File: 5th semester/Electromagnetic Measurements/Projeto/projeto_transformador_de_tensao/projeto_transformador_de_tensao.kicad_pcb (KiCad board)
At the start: 2 copper layers, 12 parts

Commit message: Update tension transformer
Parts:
- removed the REF** at (76.2, 17.8)
- removed the REF** at (33.0, 15.2)
- removed the REF** at (61.0, 27.9)
- removed the REF** at (81.3, 15.2)
- removed the REF** at (20.3, 35.6)
- removed the REF** at (71.2, 25.4)
- removed the REF** at (33.0, 22.9)
- removed the REF** at (32.9, 40.6)
- removed the REF** at (32.9, 33.0)
- added 220uF: CP_Radial_D10.0mm_P5.00mm, Capacitor_THT:CP_Radial_D10.0mm_P5.00mm, F.Cu at (44.5, 43.7)
- added 220uF: CP_Radial_D10.0mm_P5.00mm, Capacitor_THT:CP_Radial_D10.0mm_P5.00mm, F.Cu at (44.5, 38.7)
- added REF**: R_Axial_DIN0204_L3.6mm_D1.6mm_P7.62mm_Horizontal, Resistor_THT:R_Axial_DIN0204_L3.6mm_D1.6mm_P7.62mm_Horizontal, F.Cu at (47.0, 19.1)
- added REF**: D_A-405_P7.62mm_Horizontal, Diode_THT:D_A-405_P7.62mm_Horizontal, F.Cu at (25.4, 34.3)
- added REF**: D_A-405_P7.62mm_Horizontal, Diode_THT:D_A-405_P7.62mm_Horizontal, F.Cu at (25.4, 44.4)
- added REF**: Pin_D0.9mm_L10.0mm_W2.4mm_FlatFork, Connector_Pin:Pin_D0.9mm_L10.0mm_W2.4mm_FlatFork, F.Cu at (47.0, 15.2)
- added REF**: Pin_D0.9mm_L10.0mm_W2.4mm_FlatFork, Connector_Pin:Pin_D0.9mm_L10.0mm_W2.4mm_FlatFork, F.Cu at (21.6, 39.4)
- added REF**: D_A-405_P7.62mm_Horizontal, Diode_THT:D_A-405_P7.62mm_Horizontal, F.Cu at (25.5, 25.4)
- added REF**: D_A-405_P7.62mm_Horizontal, Diode_THT:D_A-405_P7.62mm_Horizontal, F.Cu at (25.5, 15.2)
- added REF**: R_Axial_DIN0204_L3.6mm_D1.6mm_P7.62mm_Horizontal, Resistor_THT:R_Axial_DIN0204_L3.6mm_D1.6mm_P7.62mm_Horizontal, F.Cu at (44.5, 22.9)
- added REF**: R_Axial_DIN0204_L3.6mm_D1.6mm_P7.62mm_Horizontal, Resistor_THT:R_Axial_DIN0204_L3.6mm_D1.6mm_P7.62mm_Horizontal, F.Cu at (29.2, 34.3)
- moved REF** 28.0 mm to (30.5, 19.1)
- moved 220uF 14.0 mm to (34.3, 26.8)
- moved REF** 1.34 mm to (21.7, 20.3)
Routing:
- net (no net): track 239.4 -> 188.0 mm

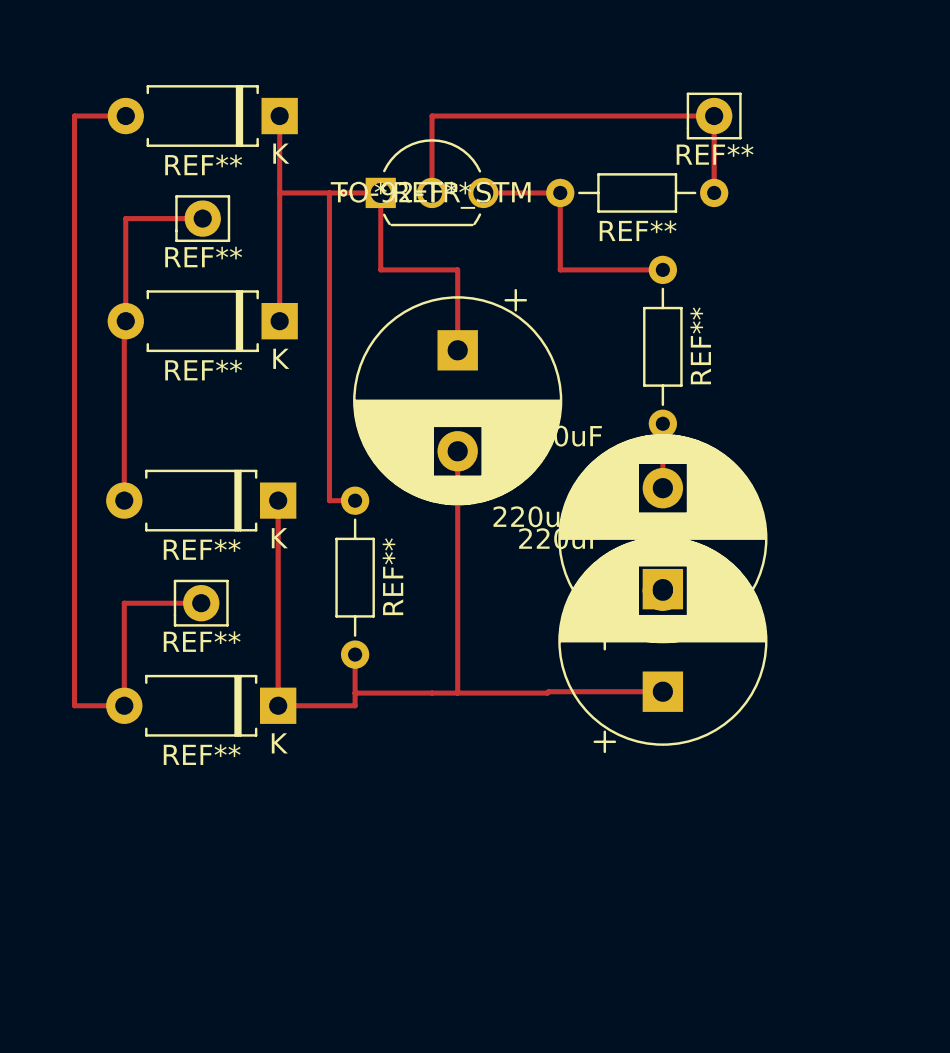
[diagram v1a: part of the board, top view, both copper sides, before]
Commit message: Final design for electromag measurements ac to dc transformer
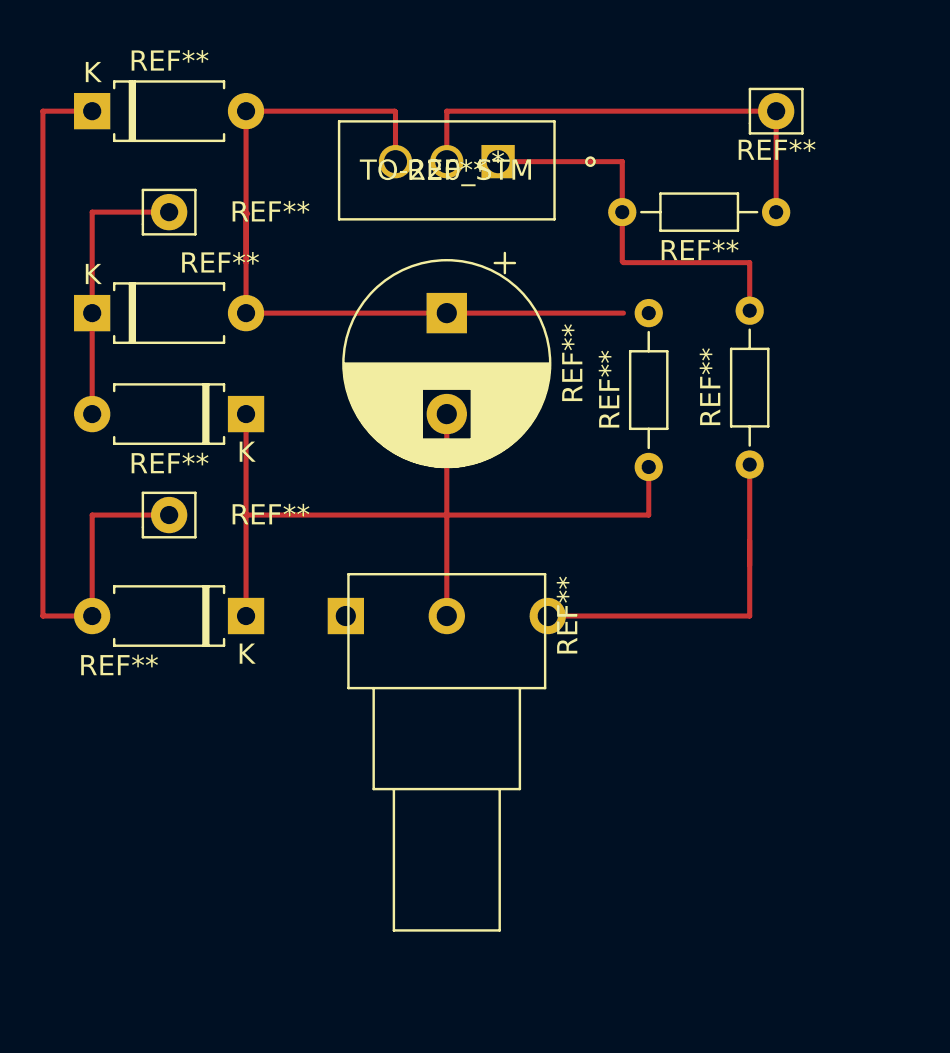
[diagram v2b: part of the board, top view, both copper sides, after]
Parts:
- removed 220uF (x3): CP_Radial_D10.0mm_P5.00mm, Capacitor_THT:CP_Radial_D10.0mm_P5.00mm
- removed the REF** at (30.5, 19.1)
- removed the REF** at (47.0, 19.1)
- removed the REF** at (25.4, 34.3)
- removed the REF** at (25.4, 44.4)
- removed the REF** at (47.0, 15.2)
- removed the REF** at (21.6, 39.4)
- removed the REF** at (25.5, 25.4)
- removed the REF** at (21.7, 20.3)
- removed the REF** at (25.5, 15.2)
- removed the REF** at (44.5, 22.9)
- removed the REF** at (29.2, 34.3)
- added REF**: D_A-405_P7.62mm_Horizontal, Diode_THT:D_A-405_P7.62mm_Horizontal, F.Cu at (23.8, 40.0)
- added REF**: R_Axial_DIN0204_L3.6mm_D1.6mm_P7.62mm_Horizontal, Resistor_THT:R_Axial_DIN0204_L3.6mm_D1.6mm_P7.62mm_Horizontal, F.Cu at (48.8, 32.5)
- added REF**: D_A-405_P7.62mm_Horizontal, Diode_THT:D_A-405_P7.62mm_Horizontal, F.Cu at (16.2, 15.0)
- added REF**: Pin_D0.9mm_L10.0mm_W2.4mm_FlatFork, Connector_Pin:Pin_D0.9mm_L10.0mm_W2.4mm_FlatFork, F.Cu at (50.1, 15.0)
- added REF**: D_A-405_P7.62mm_Horizontal, Diode_THT:D_A-405_P7.62mm_Horizontal, F.Cu at (16.2, 25.0)
- added REF**: Pin_D0.9mm_L10.0mm_W2.4mm_FlatFork, Connector_Pin:Pin_D0.9mm_L10.0mm_W2.4mm_FlatFork, F.Cu at (20.0, 20.0)
- added REF**: CP_Radial_D10.0mm_P5.00mm, Capacitor_THT:CP_Radial_D10.0mm_P5.00mm, F.Cu at (33.8, 25.0)
- added REF**: Potentiometer_Alps_RK09Y11_Single_Horizontal, Potentiometer_THT:Potentiometer_Alps_RK09Y11_Single_Horizontal, F.Cu at (31.2, 40.0)
- added REF**: R_Axial_DIN0204_L3.6mm_D1.6mm_P7.62mm_Horizontal, Resistor_THT:R_Axial_DIN0204_L3.6mm_D1.6mm_P7.62mm_Horizontal, F.Cu at (43.8, 32.6)
- added REF**: R_Axial_DIN0204_L3.6mm_D1.6mm_P7.62mm_Horizontal, Resistor_THT:R_Axial_DIN0204_L3.6mm_D1.6mm_P7.62mm_Horizontal, F.Cu at (50.1, 20.0)
- added REF**: D_A-405_P7.62mm_Horizontal, Diode_THT:D_A-405_P7.62mm_Horizontal, F.Cu at (23.8, 30.0)
- added REF**: Pin_D0.9mm_L10.0mm_W2.4mm_FlatFork, Connector_Pin:Pin_D0.9mm_L10.0mm_W2.4mm_FlatFork, F.Cu at (20.0, 35.0)
- added REF**: TO-220_STM, footprints:LM317T, F.Cu at (36.3, 17.5)
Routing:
- net (no net): track 188.0 -> 206.4 mm

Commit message: Backup point
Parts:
- added REF**: Pin_D0.9mm_L10.0mm_W2.4mm_FlatFork, Connector_Pin:Pin_D0.9mm_L10.0mm_W2.4mm_FlatFork, F.Cu at (46.2, 37.5)
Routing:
- net (no net): track 206.4 -> 211.4 mm
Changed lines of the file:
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@@
   )
   (net 0 "")
+  (footprint "Connector_Pin:Pin_D0.9mm_L10.0mm_W2.4mm_FlatFork" (layer "F.Cu")
+    (at 46.25 37.5)
+    (descr "solder Pin_ with flat fork, hole diameter 0.9mm, length 10.0mm, width 2.4mm")
+    (tags "solder Pin_ with flat fork")
+    (attr through_hole)
+    (fp_text reference "REF**" (at 0 1.95) (layer "F.SilkS")
+        (effects (font (size 1 1) (thickness 0.15)))
+    )
+    (fp_text value "Pin_D0.9mm_L10.0mm_W2.4mm_FlatFork" (at 0 -2.05) (layer "F.Fab") hide
+        (effects (font (size 1 1) (thickness 0.15)))
+    )
+    (fp_text user "${REFERENCE}" (at 0 1.95) (layer "F.Fab")
+        (effects (font (size 1 1) (thickness 0.15)))
+    )
+    (fp_line (start -1.3 -1.1) (end -1.3 0.6)
+      (stroke (width 0.12) (type solid)) (layer "F.SilkS"))
+    (fp_line (start -1.3 0.6) (end -1.3 1.1)
+      (stroke (width 0.12) (type solid)) (layer "F.SilkS"))
+    (fp_line (start -1.3 1.1) (end 1.3 1.1)
+      (stroke (width 0.12) (type solid)) (layer "F.SilkS"))
+    (fp_line (start 1.3 -1.1) (end -1.3 -1.1)
+      (stroke (width 0.12) (type solid)) (layer "F.SilkS"))
+    (fp_line (start 1.3 1.1) (end 1.3 -1.1)
+      (stroke (width 0.12) (type solid)) (layer "F.SilkS"))
+    (fp_line (start -1.7 -1.4) (end -1.7 1.4)
+      (stroke (width 0.05) (type solid)) (layer "F.CrtYd"))
+    (fp_line (start -1.7 -1.4) (end 1.7 -1.4)
+      (stroke (width 0.05) (type solid)) (layer "F.CrtYd"))
+    (fp_line (start 1.7 1.4) (end -1.7 1.4)
+      (stroke (width 0.05) (type solid)) (layer "F.CrtYd"))
+    (fp_line (start 1.7 1.4) (end 1.7 -1.4)
+      (stroke (width 0.05) (type solid)) (layer "F.CrtYd"))
+    (fp_line (start -1.2 -0.25) (end -1.2 0.25)
+      (stroke (width 0.12) (type solid)) (layer "F.Fab"))
+    (fp_line (start -1.2 0.25) (end 1.2 0.25)
+      (stroke (width 0.12) (type solid)) (layer "F.Fab"))
+    (fp_line (start 1.2 -0.25) (end -1.2 -0.25)
+      (stroke (width 0.12) (type solid)) (layer "F.Fab"))
+    (fp_line (start 1.2 0.25) (end 1.2 -0.25)
+      (stroke (width 0.12) (type solid)) (layer "F.Fab"))
+    (pad "1" thru_hole circle (at 0 0) (size 1.8 1.8) (drill 0.9) (layers "*.Cu" "*.Mask"))
+    (model "${KICAD6_3DMODEL_DIR}/Connector_Pin.3dshapes/Pin_D0.9mm_L10.0mm_W2.4mm_FlatFork.wrl"
+      (offset (xyz 0 0 0))
+      (scale (xyz 1 1 1))
+      (rotate (xyz 0 0 0))
+    )
+  )
   (footprint "Diode_THT:D_A-405_P7.62mm_Horizontal" (layer "F.Cu")
     (at 23.81 40 180)
@@
         (effects (font (size 1 1) (thickness 0.15)))
     )
+    (fp_text user "${REFERENCE}" (at 4.2 0) (layer "F.Fab")
+        (effects (font (size 1 1) (thickness 0.15)))
+    )
     (fp_text user "K" (at 0 -1.9) (layer "F.Fab")
-        (effects (font (size 1 1) (thickness 0.15)))
-    )
-    (fp_text user "${REFERENCE}" (at 4.2 0) (layer "F.Fab")
         (effects (font (size 1 1) (thickness 0.15)))
     )
@@
         (effects (font (size 1 1) (thickness 0.15)))
     )
+    (fp_text user "${REFERENCE}" (at 4.2 0) (layer "F.Fab")
+        (effects (font (size 1 1) (thickness 0.15)))
+    )
     (fp_text user "K" (at 0 -1.9) (layer "F.Fab")
-        (effects (font (size 1 1) (thickness 0.15)))
-    )
-    (fp_text user "${REFERENCE}" (at 4.2 0) (layer "F.Fab")
         (effects (font (size 1 1) (thickness 0.15)))
     )
@@
   (segment (start 42.5 22.5) (end 42.44 22.44) (width 0.25) (layer "F.Cu") (net 0))
   (segment (start 36.29 17.5) (end 42.44 17.5) (width 0.25) (layer "F.Cu") (net 0))
+  (segment (start 43.75 35) (end 43.75 37.5) (width 0.25) (layer "F.Cu") (net 0))
   (segment (start 23.81 40) (end 23.81 35) (width 0.25) (layer "F.Cu") (net 0))
   (segment (start 16.19 30) (end 16.19 25) (width 0.25) (layer "F.Cu") (net 0))
@@
   (segment (start 104.14 198.12) (end 106.68 198.12) (width 0.25) (layer "F.Cu") (net 0))
   (segment (start 31.17 15) (end 23.81 15) (width 0.25) (layer "F.Cu") (net 0))
+  (segment (start 43.75 37.5) (end 46.25 37.5) (width 0.25) (layer "F.Cu") (net 0))
   (segment (start 33.75 35) (end 33.75 30) (width 0.25) (layer "F.Cu") (net 0))
   (segment (start 16.19 35) (end 20 35) (width 0.25) (layer "F.Cu") (net 0))

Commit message: Update circuits lab report 5
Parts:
- moved Vout 0.06 mm to (50.0, 15.0)
- renumbered REF** to GND, REF** to Vin, REF** to Vout
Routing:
- net (no net): track 211.4 -> 213.7 mm
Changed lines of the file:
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@@
     (tags "solder Pin_ with flat fork")
     (attr through_hole)
-    (fp_text reference "REF**" (at 0 1.95) (layer "F.SilkS")
+    (fp_text reference "GND" (at 0 1.95) (layer "F.SilkS")
         (effects (font (size 1 1) (thickness 0.15)))
     )
@@
     (tags "Diode A-405 series Axial Horizontal pin pitch 7.62mm  length 5.2mm diameter 2.7mm")
     (attr through_hole)
-    (fp_text reference "REF**" (at 6.31 -2.47) (layer "F.SilkS")
+    (fp_text reference "REF**" (at 2.56 2.5) (layer "F.SilkS")
         (effects (font (size 1 1) (thickness 0.15)))
     )
     (fp_text value "D_A-405_P7.62mm_Horizontal" (at 3.81 2.47) (layer "F.Fab") hide
-        (effects (font (size 1 1) (thickness 0.15)))
-    )
-    (fp_text user "K" (at 0 -1.9) (layer "F.SilkS")
-        (effects (font (size 1 1) (thickness 0.15)))
-    )
-    (fp_text user "K" (at 0 -1.9) (layer "F.Fab")
         (effects (font (size 1 1) (thickness 0.15)))
     )
@@
     (tags "solder Pin_ with flat fork")
     (attr through_hole)
-    (fp_text reference "REF**" (at 5 0) (layer "F.SilkS")
+    (fp_text reference "Vin" (at -3 -1.25) (layer "F.SilkS")
         (effects (font (size 1 1) (thickness 0.15)))
     )
@@
         (effects (font (size 1 1) (thickness 0.15)))
     )
-    (fp_text user "${REFERENCE}" (at 5 0) (layer "F.Fab")
+    (fp_text user "${REFERENCE}" (at -3 -1.25) (layer "F.Fab")
         (effects (font (size 1 1) (thickness 0.15)))
     )
@@
     (tags "CP Radial series Radial pin pitch 5.00mm  diameter 10mm Electrolytic Capacitor")
     (attr through_hole)
-    (fp_text reference "REF**" (at 2.5 -6.25 90) (layer "F.SilkS")
+    (fp_text reference "REF**" (at 7.5 -5 -180) (layer "F.SilkS")
         (effects (font (size 1 1) (thickness 0.15)))
     )
@@
     (tags "Potentiometer horizontal Alps RK09Y11 Single")
     (attr through_hole)
-    (fp_text reference "REF**" (at 0 8.5 90) (layer "F.SilkS")
+    (fp_text reference "REF**" (at 2.9 6.09 180) (layer "F.SilkS")
         (effects (font (size 1 1) (thickness 0.15)))
     )
@@
     (tags "Diode A-405 series Axial Horizontal pin pitch 7.62mm  length 5.2mm diameter 2.7mm")
     (attr through_hole)
-    (fp_text reference "REF**" (at 3.81 -2.47) (layer "F.SilkS")
+    (fp_text reference "REF**" (at 2.56 -2.47) (layer "F.SilkS")
         (effects (font (size 1 1) (thickness 0.15)))
     )
@@
     (tags "solder Pin_ with flat fork")
     (attr through_hole)
-    (fp_text reference "REF**" (at 5 0) (layer "F.SilkS")
+    (fp_text reference "Vin" (at -3 -1.25) (layer "F.SilkS")
         (effects (font (size 1 1) (thickness 0.15)))
     )
@@
         (effects (font (size 1 1) (thickness 0.15)))
     )
-    (fp_text user "${REFERENCE}" (at 5 0) (layer "F.Fab")
+    (fp_text user "${REFERENCE}" (at -3 -1.25) (layer "F.Fab")
         (effects (font (size 1 1) (thickness 0.15)))
     )
@@
     (tags "Diode A-405 series Axial Horizontal pin pitch 7.62mm  length 5.2mm diameter 2.7mm")
     (attr through_hole)
-    (fp_text reference "REF**" (at 3.81 -2.47) (layer "F.SilkS")
+    (fp_text reference "REF**" (at 5.06 2.5) (layer "F.SilkS")
         (effects (font (size 1 1) (thickness 0.15)))
     )
     (fp_text value "D_A-405_P7.62mm_Horizontal" (at 3.81 2.47) (layer "F.Fab") hide
-        (effects (font (size 1 1) (thickness 0.15)))
-    )
-    (fp_text user "K" (at 0 -1.9) (layer "F.SilkS")
-        (effects (font (size 1 1) (thickness 0.15)))
-    )
-    (fp_text user "K" (at 0 -1.9) (layer "F.Fab")
         (effects (font (size 1 1) (thickness 0.15)))
     )
@@
   )
   (footprint "Connector_Pin:Pin_D0.9mm_L10.0mm_W2.4mm_FlatFork" (layer "F.Cu")
-    (at 50.06 15)
+    (at 50 15)
     (descr "solder Pin_ with flat fork, hole diameter 0.9mm, length 10.0mm, width 2.4mm")
     (tags "solder Pin_ with flat fork")
     (attr through_hole)
-    (fp_text reference "REF**" (at 0 1.95) (layer "F.SilkS")
+    (fp_text reference "Vout" (at 0 1.95) (layer "F.SilkS")
         (effects (font (size 1 1) (thickness 0.15)))
     )
@@
     (tags "Diode A-405 series Axial Horizontal pin pitch 7.62mm  length 5.2mm diameter 2.7mm")
     (attr through_hole)
-    (fp_text reference "REF**" (at 6.31 -2.47) (layer "F.SilkS")
+    (fp_text reference "REF**" (at 5.06 2.5) (layer "F.SilkS")
         (effects (font (size 1 1) (thickness 0.15)))
     )
@@
         (effects (font (size 1 1) (thickness 0.15)))
     )
-    (fp_text user "K" (at 0 -1.9) (layer "F.SilkS")
-        (effects (font (size 1 1) (thickness 0.15)))
-    )
     (fp_text user "${REFERENCE}" (at 4.2 0) (layer "F.Fab")
-        (effects (font (size 1 1) (thickness 0.15)))
-    )
-    (fp_text user "K" (at 0 -1.9) (layer "F.Fab")
         (effects (font (size 1 1) (thickness 0.15)))
     )
@@
   (segment (start 42.5 22.5) (end 42.44 22.44) (width 0.25) (layer "F.Cu") (net 0))
   (segment (start 36.29 17.5) (end 42.44 17.5) (width 0.25) (layer "F.Cu") (net 0))
+  (segment (start 43.75 33.75) (end 43.75 32.62) (width 0.25) (layer "F.Cu") (net 0))
   (segment (start 43.75 35) (end 43.75 37.5) (width 0.25) (layer "F.Cu") (net 0))
   (segment (start 23.81 40) (end 23.81 35) (width 0.25) (layer "F.Cu") (net 0))
   (segment (start 16.19 30) (end 16.19 25) (width 0.25) (layer "F.Cu") (net 0))
   (segment (start 13.75 40) (end 16.19 40) (width 0.25) (layer "F.Cu") (net 0))
-  (segment (start 48.75 40) (end 48.75 36.25) (width 0.25) (layer "F.Cu") (net 0))
+  (segment (start 48.75 40) (end 38.75 40) (width 0.25) (layer "F.Cu") (net 0))
+  (segment (start 23.93 25) (end 43.75 25) (width 0.25) (layer "F.Cu") (net 0))
   (segment (start 50.06 20) (end 50.06 15) (width 0.25) (layer "F.Cu") (net 0))
   (segment (start 104.14 198.12) (end 106.68 198.12) (width 0.25) (layer "F.Cu") (net 0))
   (segment (start 31.17 15) (end 23.81 15) (width 0.25) (layer "F.Cu") (net 0))
-  (segment (start 43.75 37.5) (end 46.25 37.5) (width 0.25) (layer "F.Cu") (net 0))
+  (segment (start 43.75 35) (end 43.75 33.75) (width 0.25) (layer "F.Cu") (net 0))
   (segment (start 33.75 35) (end 33.75 30) (width 0.25) (layer "F.Cu") (net 0))
   (segment (start 16.19 35) (end 20 35) (width 0.25) (layer "F.Cu") (net 0))
@@
   (segment (start 23.81 22.5) (end 23.81 25) (width 0.25) (layer "F.Cu") (net 0))
   (segment (start 33.75 17.5) (end 33.75 15) (width 0.25) (layer "F.Cu") (net 0))
-  (segment (start 23.89 20.08) (end 23.81 20) (width 0.25) (layer "F.Cu") (net 0))
+  (segment (start 48.75 36.25) (end 48.75 40) (width 0.25) (layer "F.Cu") (net 0))
   (segment (start 16.19 40) (end 16.19 35) (width 0.25) (layer "F.Cu") (net 0))
-  (segment (start 33.75 35) (end 23.75 35) (width 0.25) (layer "F.Cu") (net 0))
+  (segment (start 33.75 35) (end 23.81 35) (width 0.25) (layer "F.Cu") (net 0))
   (segment (start 43.75 35) (end 33.75 35) (width 0.25) (layer "F.Cu") (net 0))
-  (segment (start 43.75 35) (end 43.75 32.5) (width 0.25) (layer "F.Cu") (net 0))
   (segment (start 23.81 22.5) (end 23.81 15) (width 0.25) (layer "F.Cu") (net 0))
-  (segment (start 42.5 25) (end 23.93 25) (width 0.25) (layer "F.Cu") (net 0))
   (segment (start 42.44 17.5) (end 42.44 20) (width 0.25) (layer "F.Cu") (net 0))
-  (segment (start 31.21 17.5) (end 31.21 15.04) (width 0.25) (layer "F.Cu") (net 0))
+  (segment (start 31.21 17.5) (end 31.21 15) (width 0.25) (layer "F.Cu") (net 0))
+  (segment (start 43.75 33.75) (end 43.75 32.5) (width 0.25) (layer "F.Cu") (net 0))
   (segment (start 23.81 20) (end 23.81 15) (width 0) (layer "F.Cu") (net 0))
   (segment (start 13.75 40) (end 13.75 15) (width 0.25) (layer "F.Cu") (net 0))
@@
   (segment (start 43.63 25) (end 43.75 24.88) (width 0.25) (layer "F.Cu") (net 0))
   (segment (start 48.75 37.5) (end 48.75 32.5) (width 0.25) (layer "F.Cu") (net 0))
-  (segment (start 48.75 40) (end 38.75 40) (width 0.25) (layer "F.Cu") (net 0))
   (segment (start 50 19.94) (end 50.06 20) (width 0.25) (layer "F.Cu") (net 0))
   (segment (start 33.75 35) (end 33.75 40) (width 0.25) (layer "F.Cu") (net 0))
+  (segment (start 43.75 37.5) (end 46.25 37.5) (width 0.25) (layer "F.Cu") (net 0))
   (segment (start 23.93 24.88) (end 23.81 25) (width 0.25) (layer "F.Cu") (net 0))
   (segment (start 16.25 40) (end 16.19 40) (width 0.25) (layer "F.Cu") (net 0))
